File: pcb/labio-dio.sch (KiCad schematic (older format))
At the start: 100 parts, among them P601 CONN_01X02, P602 CONN_01X02, P603 CONN_01X04, P604 CONN_01X02, P605 CONN_01X03, P606 CONN_01X03, P607 CONN_01X05, P608 CONN_01X05, Q601 Q_NMOS_GSD, Q602 Q_NMOS_GSD, Q603 Q_NMOS_GSD, Q604 Q_NMOS_GSD, Q605 Q_NMOS_GSD, Q606 Q_NMOS_GSD, Q607 Q_NMOS_GSD, Q608 Q_NMOS_GSD, Q609 Q_NMOS_GSD, Q610 Q_NMOS_GSD, Q611 Q_NMOS_GSD, Q612 Q_NMOS_GSD, Q613 Q_NMOS_GSD, SW601 DIP_SWITCH_X04, SW602 DIP_SWITCH_X04, SW603 DIP_SWITCH_X04, SW604 DIP_SWITCH_X04, SW605 ROT_ENC, SW606 DIP_SWITCH_X04, U601 L298P

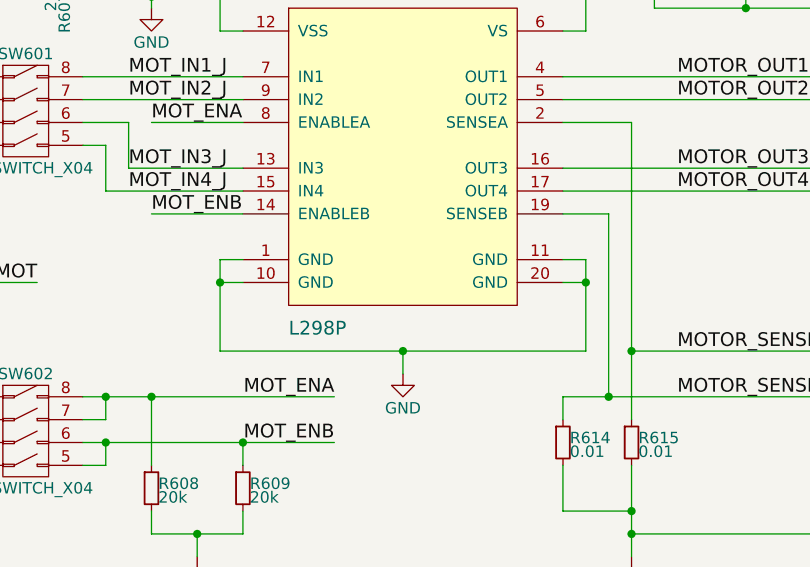
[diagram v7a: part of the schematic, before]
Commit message: finish rerouting for new parts
* fix adc power supply nets
* redo adc layout
* move motor controller up to make space for headers
* add motor controller heatsink mount
* fix motor controller ground pad net

todo:
* silkscreen
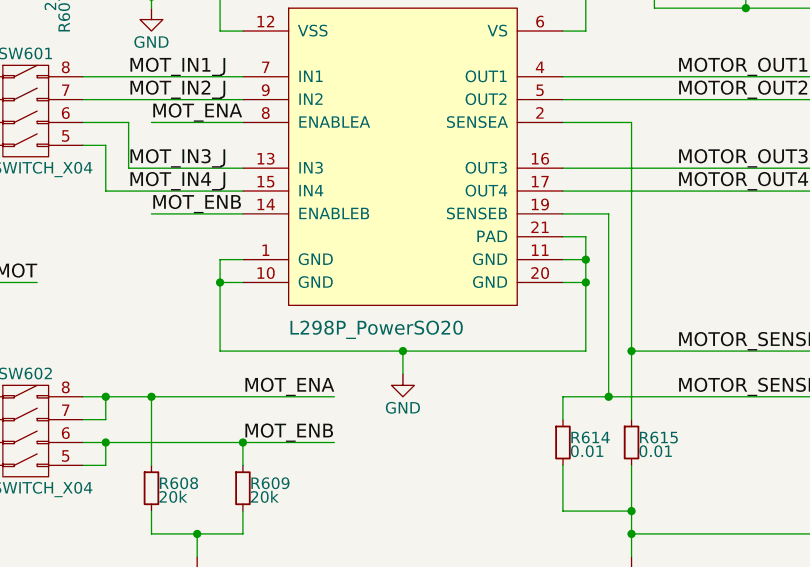
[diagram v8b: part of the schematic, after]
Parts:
- removed U601: L298P, labio-special:PowerSO20, symbol L298P
- added U601: L298P_PowerSO20, labio-special:PowerSO20, symbol L298P_PowerSO20
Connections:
- net GND: now also U601.1 (GND), U601.10 (GND), U601.11 (GND), U601.20 (GND), U601.21 (PAD)
- net MOTOR_OUT1: now also U601.4 (OUT1)
- net MOTOR_OUT2: now also U601.5 (OUT2)
- net MOTOR_OUT3: now also U601.16 (OUT3)
- net MOTOR_OUT4: now also U601.17 (OUT4)
- net MOTOR_SENSEA: now also U601.2 (SENSEA)
- net MOTOR_SENSEB: now also U601.19 (SENSEB)
- net MOT_ENA: now also U601.8 (ENABLEA)
- net MOT_ENB: now also U601.14 (ENABLEB)
- net MOT_IN1_J: now also U601.7 (IN1)
- net MOT_IN2_J: now also U601.9 (IN2)
- net MOT_IN3_J: now also U601.13 (IN3)
- net MOT_IN4_J: now also U601.15 (IN4)
- net VDD_MOT: now also U601.12 (VSS)
- net VS_MOTOR: now also U601.6 (VS)
